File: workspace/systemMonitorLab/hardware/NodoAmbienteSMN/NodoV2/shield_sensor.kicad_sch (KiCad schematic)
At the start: 4 parts, among them J4 Molex_Sensor_BMP280, J5 Molex_Sensor_DHT22, U3 DHT22, U4 Bmp280Module

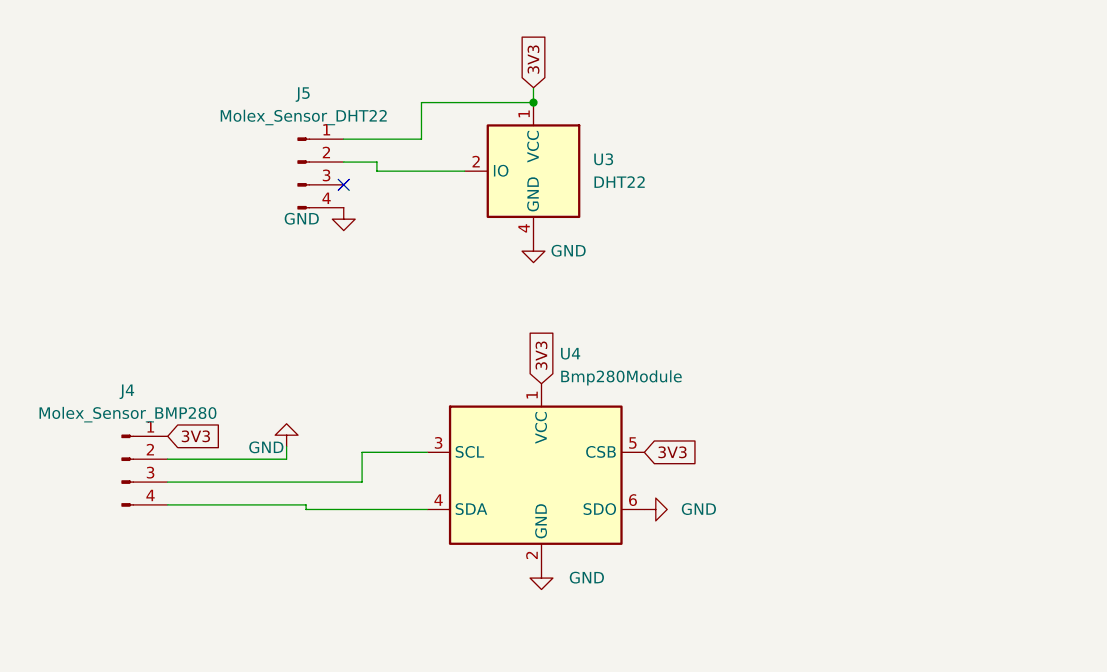
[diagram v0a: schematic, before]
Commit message: Se termino de generar el diseño de la placa shield_main_board.
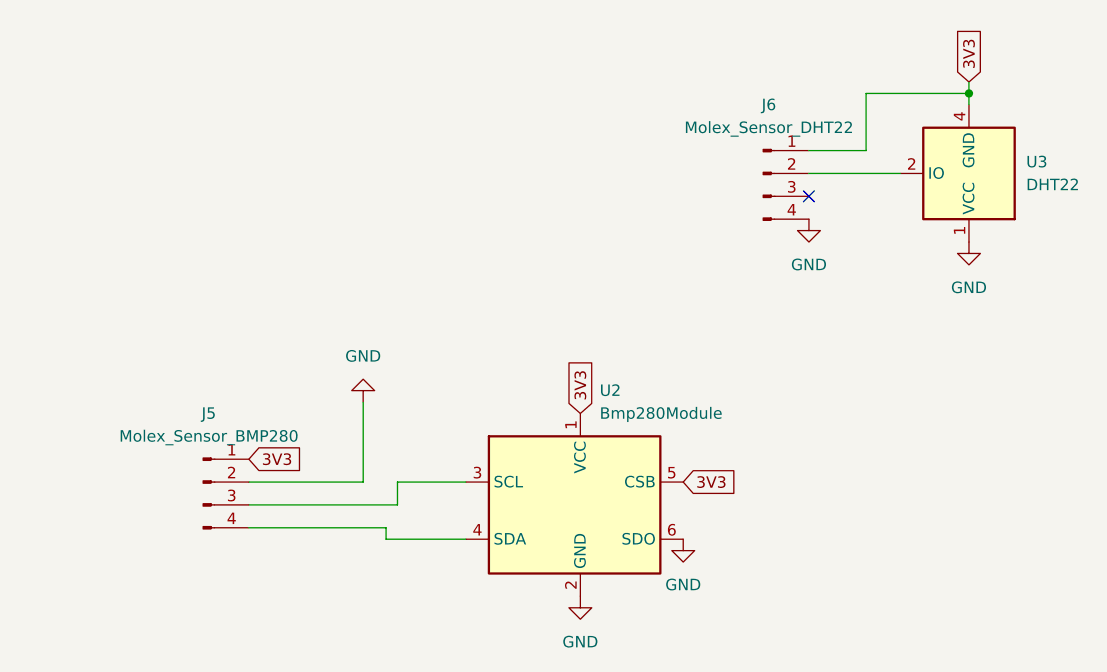
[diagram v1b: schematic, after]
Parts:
- removed J4: Molex_Sensor_BMP280, Connector_PinHeader_2.54mm:PinHeader_1x04_P2.54mm_Horizontal, symbol Connector:Conn_01x04_Male
- removed J5: Molex_Sensor_DHT22, Connector_PinHeader_2.54mm:PinHeader_1x04_P2.54mm_Horizontal, symbol Connector:Conn_01x04_Male
- removed U3: DHT22, Sensor:Aosong_DHT11_5.5x12.0_P2.54mm, symbol New_Library:DHT22
- removed U4: Bmp280Module, Modulos:BMP280_Module, symbol New_Library:Bmp280Module
- added J5: Molex_Sensor_BMP280, Connector_PinHeader_2.54mm:PinHeader_1x04_P2.54mm_Horizontal, symbol Connector:Conn_01x04_Pin
- added J6: Molex_Sensor_DHT22, Connector_PinHeader_2.54mm:PinHeader_1x04_P2.54mm_Horizontal, symbol Connector:Conn_01x04_Pin
- added U2: Bmp280Module, Sensors_commercial:BMP280_Module, symbol Sensores_comerciales:Bmp280Module
- added U3: DHT22, Sensor:Aosong_DHT11_5.5x12.0_P2.54mm, symbol Sensores_comerciales:DHT22
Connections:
- net 3V3: now also J5.1 (Pin_1), J6.1 (Pin_1), U2.1 (VCC), U2.5 (CSB), U3.4 (GND)
- net GND: now also J5.2 (Pin_2), J6.4 (Pin_4), U2.2 (GND), U2.6 (SDO), U3.1 (VCC)
- new net: J6.2 (Pin_2), U3.2 (IO)
- new net: J5.3 (Pin_3), U2.3 (SCL)
- new net: J5.4 (Pin_4), U2.4 (SDA)
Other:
- company: (none) -> Servicio Meteorológico Nacional (SMN)
- title: (none) -> shield_sensors_nodo

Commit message: Tareas Realizadas: 	- Se corrije la disposicion de los conectores, para que el cable 	  quede derecho en su construccion se tiene que invertir el 	  orden de los pines en las placas led_status y sensors. 	- Se Cambio el ancho de las pistas que atraviesan a los 	  resistores SMD de 30 a 25 mils. 	- Se esta transmitiendo al sevirdor nginx por el puerto 80. Tareas proximas: 	- Se debe Contruir las placas y realizar pruebas. 	- Modificar el firmware para que los led envien los estados por 	  PWM para el LED dual. y On - OFF para el Led simple. 	- Se debe agregar un filtro para que los datos que tengan una 	  varianza mayor a un valor x no se transmitan. 	- Se debe agregar un retardo para que no se transmitan los datos 	  de inicio del barometro, ya que siempre marcan un valor 	  alredeor de 700 hPa.
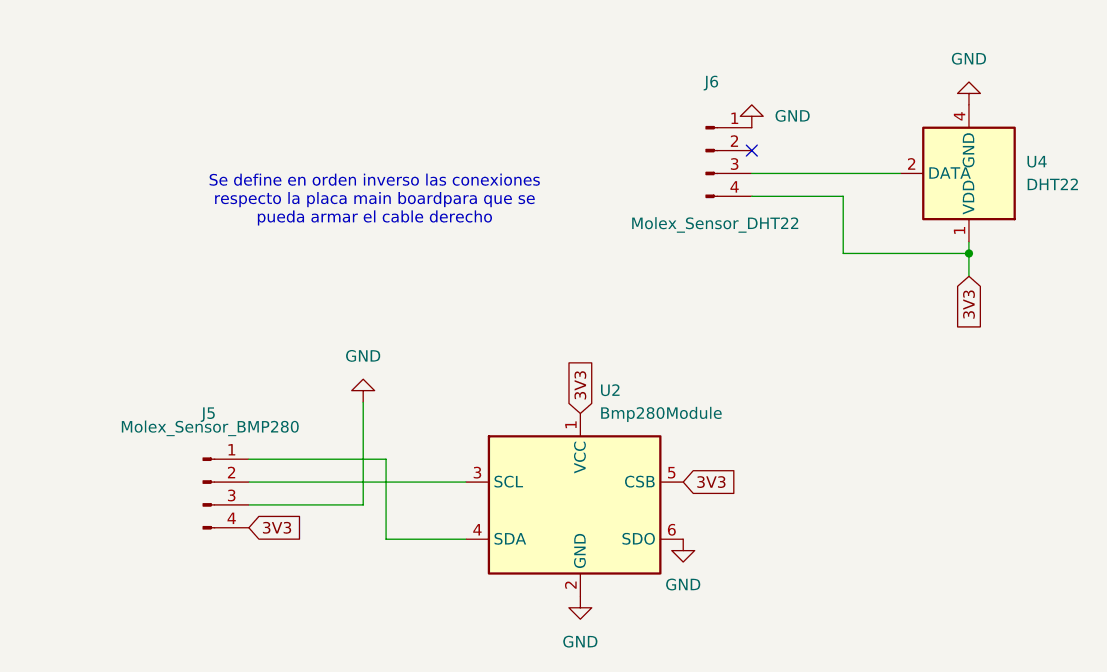
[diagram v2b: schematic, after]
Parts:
- removed U3: DHT22, Sensor:Aosong_DHT11_5.5x12.0_P2.54mm, symbol Sensores_comerciales:DHT22
- added U4: DHT22, Sensor:Aosong_DHT11_5.5x12.0_P2.54mm, symbol Sensor:DHT11
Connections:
- net 3V3: now also J5.4 (Pin_4), J6.4 (Pin_4), U4.1 (VDD); no longer J5.1 (Pin_1), J6.1 (Pin_1)
- net GND: now also J5.3 (Pin_3), J6.1 (Pin_1), U4.4 (GND); no longer J5.2 (Pin_2), J6.4 (Pin_4)
- net at U2.3 (SCL): now also J5.2 (Pin_2); no longer J5.3 (Pin_3)
- net at U2.4 (SDA): now also J5.1 (Pin_1); no longer J5.4 (Pin_4)
- net at J6.3 (Pin_3): now also U4.2 (DATA)
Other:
- note added: "Se define en orden inverso las conexiones respecto la placa main boardpara que se pueda armar el cable derecho"

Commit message: Se mejora el plano de masa del PCB
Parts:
- removed U2: Bmp280Module, Sensors_commercial:BMP280_Module, symbol Sensores_comerciales:Bmp280Module
- added U2: Bmp280Module, Modulos_comerciales:BMP280_Module, symbol simbolos:Bmp280Module
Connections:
- net 3V3: now also U2.1 (VCC), U2.5 (CSB)
- net GND: now also U2.2 (GND), U2.6 (SDO)
- net at J5.1 (Pin_1): now also U2.4 (SDA)
- net at J5.2 (Pin_2): now also U2.3 (SCL)
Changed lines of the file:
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@@
+	)
+	(symbol
+		(lib_id "simbolos:Bmp280Module")
+		(at 142.24 110.49 0)
+		(unit 1)
+		(exclude_from_sim no)
+		(in_bom yes)
+		(on_board yes)
+		(dnp no)
+		(fields_autoplaced yes)
+		(property "Reference" "U2"
+			(at 144.3833 96.52 0)
+			(effects
+				(font
+					(size 1.27 1.27)
+				)
+				(justify left)
+			)
+		)
+		(property "Value" "Bmp280Module"
+			(at 144.3833 99.06 0)
+			(effects
+				(font
+					(size 1.27 1.27)
+				)
+				(justify left)
+			)
+		)
+		(property "Footprint" "Modulos_comerciales:BMP280_Module"
+			(at 181.61 132.08 0)
+			(effects
+				(font
+					(size 1.27 1.27)
+				)
+				(hide yes)
+			)
+		)
+		(property "Datasheet" ""
+			(at 138.43 111.76 0)
+			(effects
+				(font
+					(size 1.27 1.27)
+				)
+				(hide yes)
+			)
+		)
+		(property "Description" ""
+			(at 142.24 110.49 0)
+			(effects
+				(font
+					(size 1.27 1.27)
+				)
+				(hide yes)
+			)
+		)
+		(pin "5"
+		)
+		(pin "6"
+		)
+		(pin "4"
+		)
+		(pin "1"
+		)
+		(pin "3"
+		)
+		(pin "2"
+		)
+		(instances
+			(project ""
+				(path "/31567b71-44a6-4f20-978f-6760a129c7a5/a5c8404b-c871-4957-8f0c-905335996a80"
+					(reference "U2")
+					(unit 1)
+				)
+			)
+		)
 	)
 	(symbol
@@
 					(unit 1)
 				)
-			)
-		)
-	)
-	(symbol
-		(lib_id "Sensores_comerciales:Bmp280Module")
-		(at 142.24 110.49 0)
-		(unit 1)
-		(exclude_from_sim no)
-		(in_bom yes)
-		(on_board yes)
-		(dnp no)
-		(fields_autoplaced yes)
-		(property "Reference" "U2"
-			(at 144.3833 96.52 0)
-			(effects
-				(font
-					(size 1.27 1.27)
-				)
-				(justify left)
-			)
-		)
-		(property "Value" "Bmp280Module"
-			(at 144.3833 99.06 0)
-			(effects
-				(font
-					(size 1.27 1.27)
-				)
-				(justify left)
-			)
-		)
-		(property "Footprint" "Sensors_commercial:BMP280_Module"
-			(at 181.61 132.08 0)
-			(effects
-				(font
-					(size 1.27 1.27)
-				)
-				(hide yes)
-			)
-		)
-		(property "Datasheet" ""
-			(at 138.43 111.76 0)
-			(effects
-				(font
-					(size 1.27 1.27)
-				)
-				(hide yes)
-			)
-		)
-		(property "Description" ""
-			(at 142.24 110.49 0)
-			(effects
-				(font
-					(size 1.27 1.27)
-				)
-				(hide yes)
-			)
-		)
-		(pin "4"
-		)
-		(pin "3"
-		)
-		(pin "6"
-		)
-		(pin "2"
-		)
-		(pin "1"
-		)
-		(pin "5"
-		)
-		(instances
-			(project ""
-				(path "/31567b71-44a6-4f20-978f-6760a129c7a5/a5c8404b-c871-4957-8f0c-905335996a80"
-					(reference "U2")
-					(unit 1)
-				)
